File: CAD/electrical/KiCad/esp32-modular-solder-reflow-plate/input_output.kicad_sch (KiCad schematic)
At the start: 55 parts, among them J2 HEATER P, J3 HEATER N, J7 PWR_IN

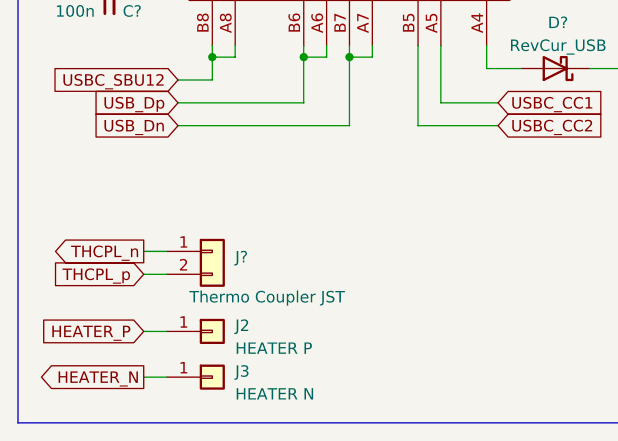
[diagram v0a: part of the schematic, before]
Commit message: - CAD: library clean up, routing improvements, new heat bed terminal
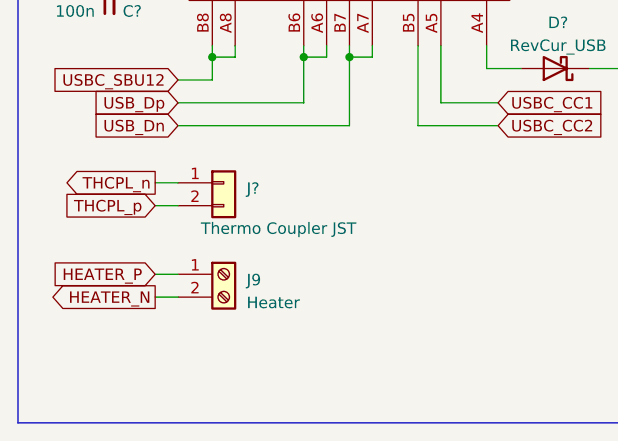
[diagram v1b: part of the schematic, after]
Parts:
- removed J2: HEATER P, Connector_Pin:Pin_D1.3mm_L11.0mm, symbol Connector_Generic:Conn_01x01
- removed J3: HEATER N, Connector_Pin:Pin_D1.3mm_L11.0mm, symbol Connector_Generic:Conn_01x01
- added J9: Heater, TerminalBlock:TerminalBlock_bornier-2_P5.08mm, symbol Connector:Screw_Terminal_01x02
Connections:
- net HEATER_N: now also J9.2 (Pin_2)
- net HEATER_P: now also J9.1 (Pin_1)
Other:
- moved on the sheet: J?
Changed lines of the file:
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@@
-(kicad_sch (version 20230221) (generator eeschema)
+(kicad_sch (version 20230409) (generator eeschema)
   (paper "A4")
   (title_block
@@
     (stroke (width 0) (type default))
   )
-  (wire (pts (xy 29.21 172.72) (xy 31.75 172.72))
+  (wire (pts (xy 30.48 165.1) (xy 33.02 165.1))
     (stroke (width 0) (type default))
   )
@@
     (stroke (width 0) (type default))
   )
-  (wire (pts (xy 29.21 175.26) (xy 31.75 175.26))
+  (wire (pts (xy 30.48 167.64) (xy 33.02 167.64))
     (stroke (width 0) (type default))
   )
@@
     (stroke (width 0) (type default))
   )
-  (wire (pts (xy 29.21 181.61) (xy 31.75 181.61))
+  (wire (pts (xy 30.48 175.26) (xy 33.02 175.26))
     (stroke (width 0) (type default))
   )
@@
     (stroke (width 0) (type default))
   )
-  (wire (pts (xy 29.21 186.69) (xy 31.75 186.69))
+  (wire (pts (xy 30.48 177.8) (xy 33.02 177.8))
     (stroke (width 0) (type default))
   )
@@
     (stroke (width 0) (type default))
   )
-  (text "BUTTONS\n" (at 17.78 19.05 0)
+  (text "BUTTONS\n" (exclude_from_sim no)
+ (at 17.78 19.05 0)
     (effects (font (size 1.27 1.27) (thickness 0.254) bold) (justify left bottom))
   )
-  (text "SD-CARD\n" (at 17.78 73.66 0)
+  (text "SD-CARD\n" (exclude_from_sim no)
+ (at 17.78 73.66 0)
     (effects (font (size 1.27 1.27) (thickness 0.254) bold) (justify left bottom))
   )
-  (text "CONNECTORS\n" (at 30.48 123.19 0)
+  (text "CONNECTORS\n" (exclude_from_sim no)
+ (at 30.48 123.19 0)
     (effects (font (size 1.27 1.27) (thickness 0.254) bold) (justify right bottom))
   )
-  (text "LEDS" (at 135.89 19.05 0)
+  (text "LEDS" (exclude_from_sim no)
+ (at 135.89 19.05 0)
     (effects (font (size 1.27 1.27) (thickness 0.254) bold) (justify left bottom))
   )
-  (text "Ensure to use the \ncorrect load resistors\nfor CC1 and 2!\n"
+  (text "Ensure to use the \ncorrect load resistors\nfor CC1 and 2!\n" (exclude_from_sim no)
     (at 72.39 144.78 0)
     (effects (font (size 1.27 1.27) (thickness 0.254) bold (color 255 0 15 1)) (justify left bottom))
@@
     )
   )
-  (global_label "THCPL_n" (shape output) (at 29.21 172.72 180) (fields_autoplaced)
+  (global_label "THCPL_n" (shape output) (at 30.48 165.1 180) (fields_autoplaced)
     (effects (font (size 1.27 1.27)) (justify right))
-    (property "Intersheetrefs" "${INTERSHEET_REFS}" (at 18.3214 172.72 0)
+    (property "Intersheetrefs" "${INTERSHEET_REFS}" (at 19.5914 165.1 0)
       (effects (font (size 1.27 1.27)) (justify right) hide)
     )
@@
     )
   )
-  (global_label "HEATER_P" (shape input) (at 29.21 181.61 180) (fields_autoplaced)
+  (global_label "HEATER_P" (shape input) (at 30.48 175.26 180) (fields_autoplaced)
     (effects (font (size 1.27 1.27)) (justify right))
-    (property "Intersheetrefs" "${INTERSHEET_REFS}" (at 17.1119 181.61 0)
+    (property "Intersheetrefs" "${INTERSHEET_REFS}" (at 18.3819 175.26 0)
       (effects (font (size 1.27 1.27)) (justify right) hide)
     )
@@
     )
   )
-  (global_label "THCPL_p" (shape input) (at 29.21 175.26 180) (fields_autoplaced)
+  (global_label "THCPL_p" (shape input) (at 30.48 167.64 180) (fields_autoplaced)
     (effects (font (size 1.27 1.27)) (justify right))
-    (property "Intersheetrefs" "${INTERSHEET_REFS}" (at 18.3214 175.26 0)
+    (property "Intersheetrefs" "${INTERSHEET_REFS}" (at 19.5914 167.64 0)
       (effects (font (size 1.27 1.27)) (justify right) hide)
     )
@@
     )
   )
-  (global_label "HEATER_N" (shape output) (at 29.21 186.69 180) (fields_autoplaced)
+  (global_label "HEATER_N" (shape output) (at 30.48 177.8 180) (fields_autoplaced)
     (effects (font (size 1.27 1.27)) (justify right))
-    (property "Intersheetrefs" "${INTERSHEET_REFS}" (at 17.0514 186.69 0)
+    (property "Intersheetrefs" "${INTERSHEET_REFS}" (at 18.3214 177.8 0)
       (effects (font (size 1.27 1.27)) (justify right) hide)
     )
@@
     )
   )
-  (symbol (lib_id "Connector_Generic:Conn_01x01") (at 36.83 186.69 0) (unit 1)
-    (in_bom yes) (on_board yes) (dnp no) (fields_autoplaced)
-    (property "Reference" "J3" (at 39.37 186.055 0)
-      (effects (font (size 1.27 1.27)) (justify left))
-    )
-    (property "Value" "HEATER N" (at 39.37 188.595 0)
-      (effects (font (size 1.27 1.27)) (justify left))
-    )
-    (property "Footprint" "Connector_Pin:Pin_D1.3mm_L11.0mm" (at 36.83 186.69 0)
-      (effects (font (size 1.27 1.27)) hide)
-    )
-    (property "Datasheet" "~" (at 36.83 186.69 0)
-      (effects (font (size 1.27 1.27)) hide)
-    )
-    (pin "1")
-    (instances
-      (project "esp32-modular-solder-reflow-plate"
-        (path "/33f3a99a-8df0-41a5-be2d-1e3400ca68bb/9103847b-7285-41f5-846d-96de7eb793c2"
-          (reference "J3") (unit 1)
-        )
-      )
-    )
-  )
   (symbol (lib_id "Device:D_Schottky") (at 74.93 152.4 180) (unit 1)
     (in_bom yes) (on_board yes) (dnp no) (fields_autoplaced)
@@
     )
   )
-  (symbol (lib_id "Connector_Generic:Conn_01x01") (at 36.83 181.61 0) (unit 1)
-    (in_bom yes) (on_board yes) (dnp no) (fields_autoplaced)
-    (property "Reference" "J2" (at 39.37 180.975 0)
-      (effects (font (size 1.27 1.27)) (justify left))
-    )
-    (property "Value" "HEATER P" (at 39.37 183.515 0)
-      (effects (font (size 1.27 1.27)) (justify left))
-    )
-    (property "Footprint" "Connector_Pin:Pin_D1.3mm_L11.0mm" (at 36.83 181.61 0)
-      (effects (font (size 1.27 1.27)) hide)
-    )
-    (property "Datasheet" "~" (at 36.83 181.61 0)
-      (effects (font (size 1.27 1.27)) hide)
-    )
-    (pin "1")
-    (instances
-      (project "esp32-modular-solder-reflow-plate"
-        (path "/33f3a99a-8df0-41a5-be2d-1e3400ca68bb/9103847b-7285-41f5-846d-96de7eb793c2"
-          (reference "J2") (unit 1)
-        )
-      )
-    )
-  )
   (symbol (lib_id "power:GND") (at 100.33 77.47 0) (unit 1)
     (in_bom yes) (on_board yes) (dnp no)
@@
     )
   )
-  (symbol (lib_id "Connector_Generic:Conn_01x02") (at 36.83 172.72 0) (unit 1)
+  (symbol (lib_id "Connector_Generic:Conn_01x02") (at 38.1 165.1 0) (unit 1)
     (in_bom yes) (on_board yes) (dnp no)
-    (property "Reference" "J?" (at 39.37 173.355 0)
+    (property "Reference" "J?" (at 40.64 165.735 0)
       (effects (font (size 1.27 1.27)) (justify left))
     )
-    (property "Value" "Thermo Coupler JST" (at 34.29 177.8 0)
+    (property "Value" "Thermo Coupler JST" (at 35.56 170.18 0)
       (effects (font (size 1.27 1.27)) (justify left))
     )
-    (property "Footprint" "Connector_JST:JST_XH_B2B-XH-A_1x02_P2.50mm_Vertical" (at 36.83 172.72 0)
+    (property "Footprint" "Connector_JST:JST_XH_B2B-XH-A_1x02_P2.50mm_Vertical" (at 38.1 165.1 0)
       (effects (font (size 1.27 1.27)) hide)
     )
-    (property "Datasheet" "~" (at 36.83 172.72 0)
+    (property "Datasheet" "~" (at 38.1 165.1 0)
       (effects (font (size 1.27 1.27)) hide)
     )
@@
         )
       )
+    )
+  )
+  (symbol (lib_id "Connector:Screw_Terminal_01x02") (at 38.1 175.26 0) (unit 1)
+    (in_bom yes) (on_board yes) (dnp no) (fields_autoplaced)
+    (property "Reference" "J9" (at 40.64 175.895 0)
+      (effects (font (size 1.27 1.27)) (justify left))
+    )
+    (property "Value" "Heater" (at 40.64 178.435 0)
+      (effects (font (size 1.27 1.27)) (justify left))
+    )
+    (property "Footprint" "TerminalBlock:TerminalBlock_bornier-2_P5.08mm" (at 38.1 175.26 0)
+      (effects (font (size 1.27 1.27)) hide)
+    )
+    (property "Datasheet" "~" (at 38.1 175.26 0)
+      (effects (font (size 1.27 1.27)) hide)
+    )
+    (pin "1")
+    (pin "2")
+    (instances
+      (project "esp32-modular-solder-reflow-plate"
+        (path "/33f3a99a-8df0-41a5-be2d-1e3400ca68bb/9103847b-7285-41f5-846d-96de7eb793c2"
+          (reference "J9") (unit 1)
+        )
+      )

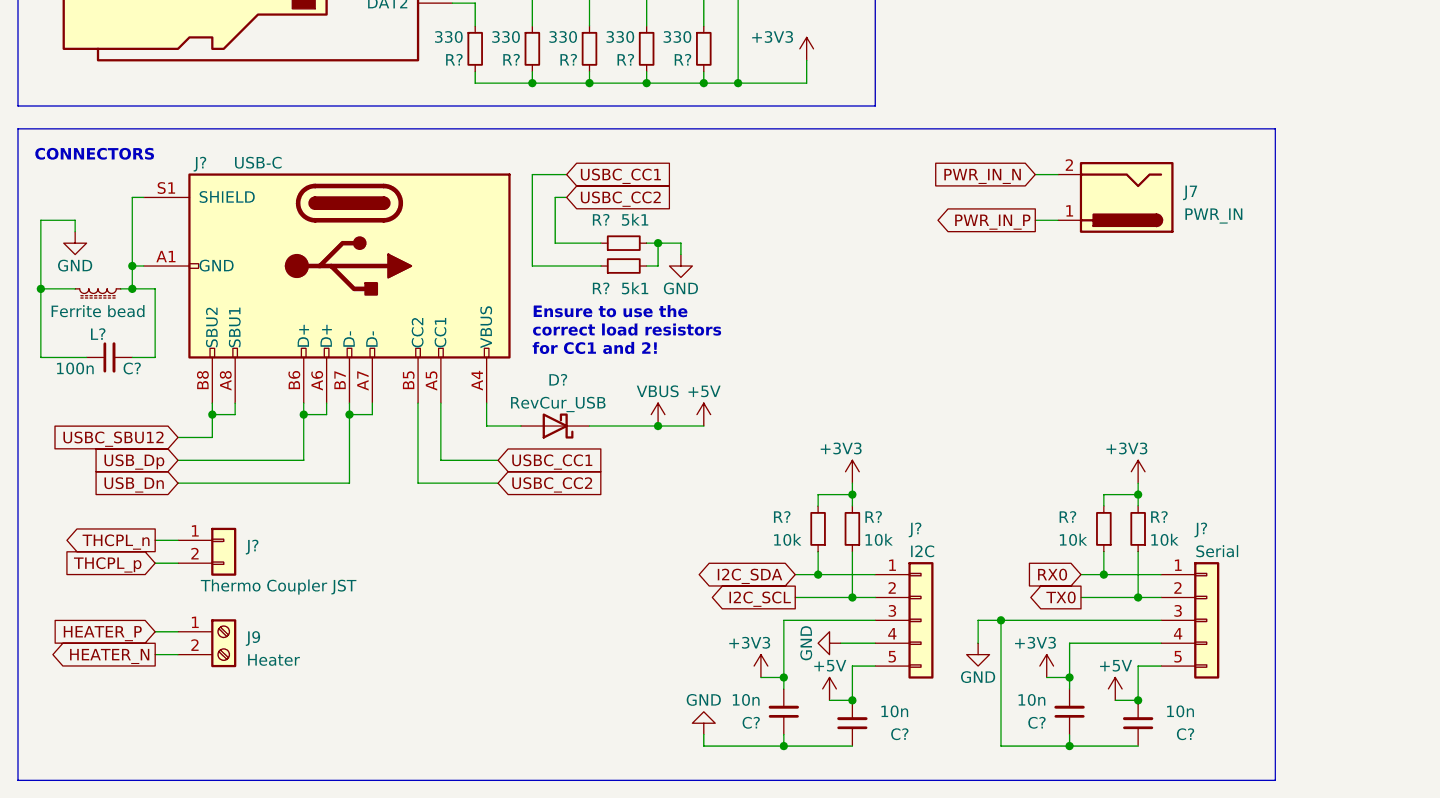
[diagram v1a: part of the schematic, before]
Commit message: - cad: added USB d+ and d- pull up and pull down options; optimized overall component layout; improved silkscreens
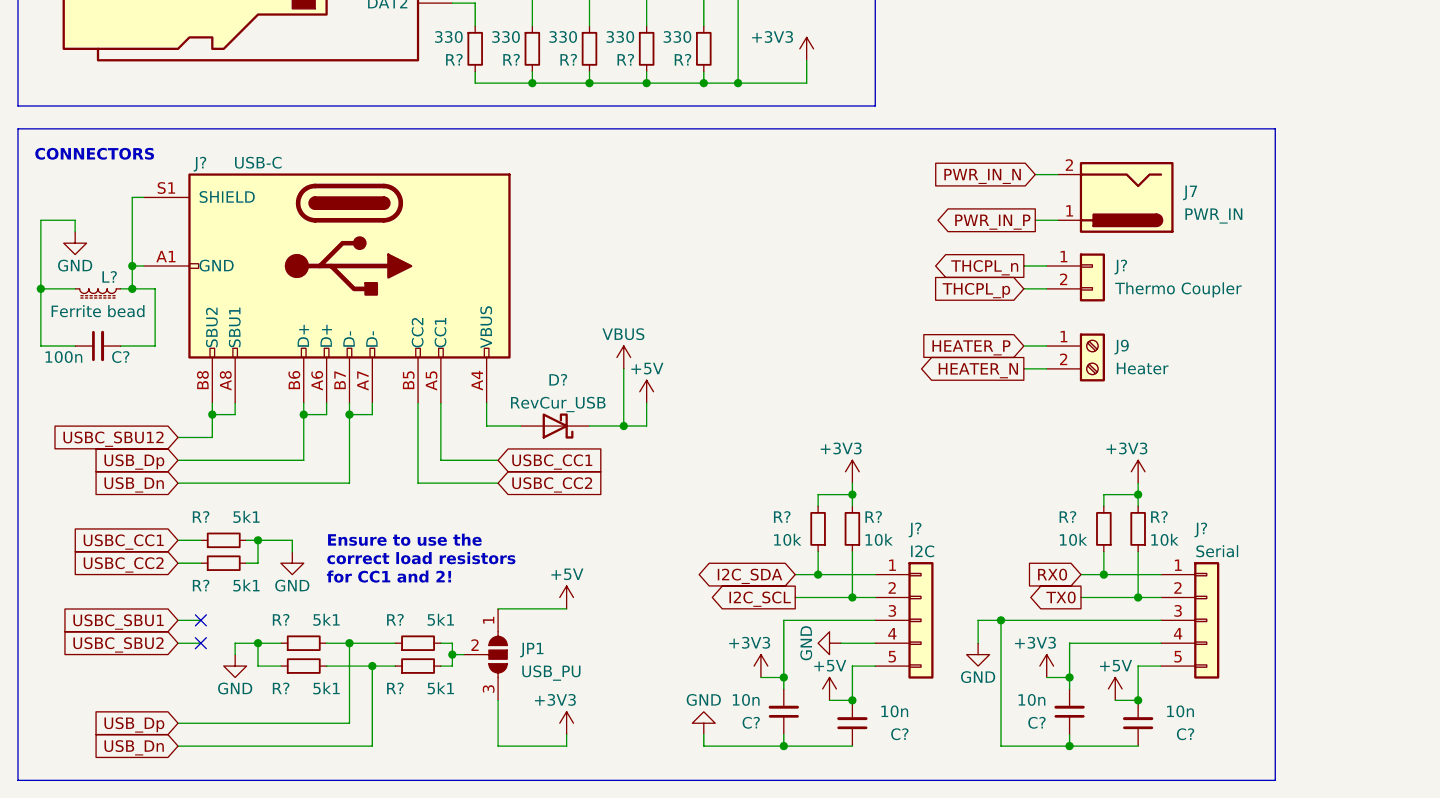
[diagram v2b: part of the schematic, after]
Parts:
- added JP1: USB_PU, Jumper:SolderJumper-3_P1.3mm_Open_RoundedPad1.0x1.5mm, symbol Jumper:SolderJumper_3_Open
- added R? (x4): 5k1, Resistor_SMD:R_0603_1608Metric_Pad0.98x0.95mm_HandSolder, symbol Device:R_Small
- J?: value Thermo Coupler JST -> Thermo Coupler
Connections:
- net +3V3: now also JP1.3 (B)
- net +5V: now also JP1.1 (A)
- net GND: now also R?.1, R?.1
- net USB_Dn: now also R?.1, R?.2
- net USB_Dp: now also R?.1, R?.2
- new net: JP1.2 (C), R?.2, R?.2
- no-connect marks 1 -> 3
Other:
- moved on the sheet: C?, J9, J?, R?

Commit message: - cad: improved routing; added VIN voltage monitoring capability
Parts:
- renumbered J9 to J5, J7 to J6

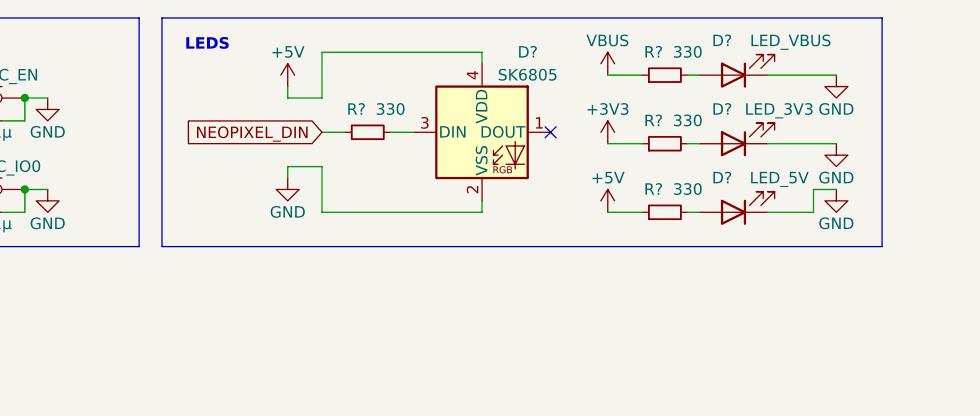
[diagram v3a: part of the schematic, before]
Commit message: - cad: swapped WS2812 against SK6812Mini
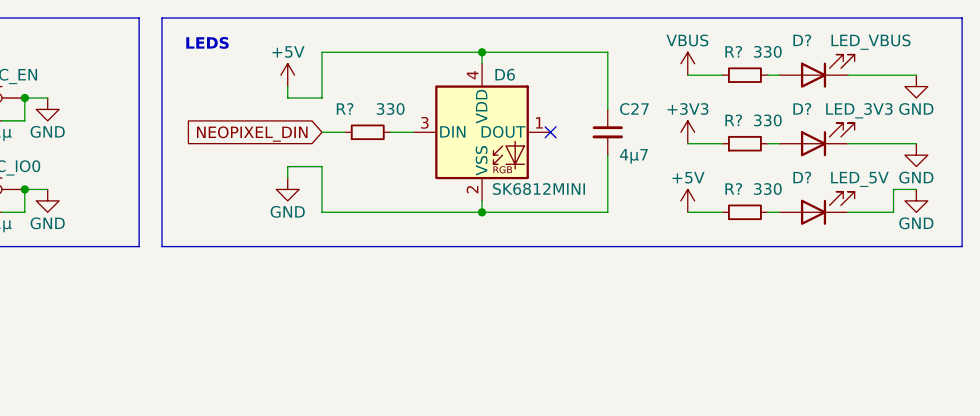
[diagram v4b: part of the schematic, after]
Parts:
- removed D?: SK6805, LED_SMD:LED_RGB_5050-6, symbol LED:SK6805
- added C27: 4µ7, Capacitor_SMD:C_0603_1608Metric_Pad1.08x0.95mm_HandSolder, symbol Device:C_Small
- added D6: SK6812MINI, LED_SMD:LED_SK6812MINI_PLCC4_3.5x3.5mm_P1.75mm, symbol LED:SK6812MINI
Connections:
- net +5V: now also C27.1, D6.4 (VDD)
- net GND: now also C27.2, D6.2 (VSS)
- net at R?.2: now also D6.3 (DIN)
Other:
- moved on the sheet: D?, R?

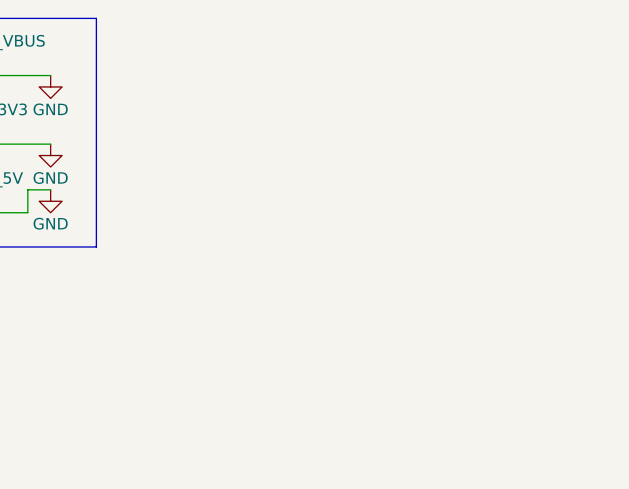
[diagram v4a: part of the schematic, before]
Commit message: - cad: added a buzzer control output
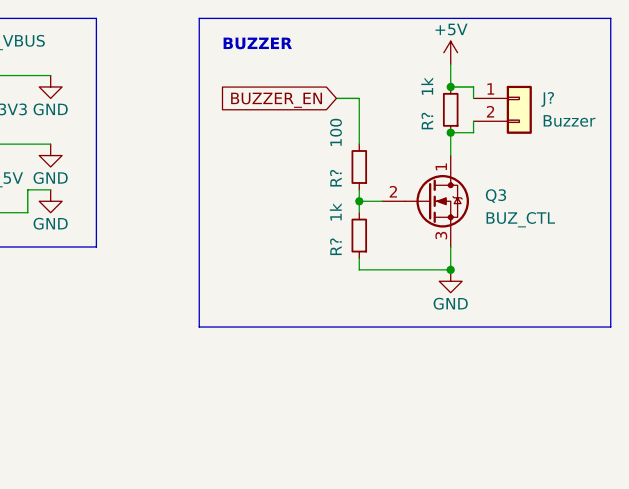
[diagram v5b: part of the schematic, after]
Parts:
- added J?: Buzzer, Connector_JST:JST_XH_B2B-XH-A_1x02_P2.50mm_Vertical, symbol Connector_Generic:Conn_01x02
- added Q3: BUZ_CTL, Package_TO_SOT_SMD:SOT-23, symbol Device:Q_NMOS_DGS
- added R? (x2): 1k, Resistor_SMD:R_0603_1608Metric_Pad0.98x0.95mm_HandSolder, symbol Device:R_Small
- added R?: 100, Resistor_SMD:R_0603_1608Metric_Pad0.98x0.95mm_HandSolder, symbol Device:R_Small
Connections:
- net +5V: now also J?.1 (Pin_1), R?.2
- net GND: now also Q3.3 (S), R?.1
- new net: J?.2 (Pin_2), Q3.1 (D), R?.1
- new net: Q3.2 (G), R?.1, R?.2
- new net BUZZER_EN: R?.2
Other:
- note added: "BUZZER"
